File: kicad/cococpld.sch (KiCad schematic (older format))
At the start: 25 parts, among them P1 COCOBUS, P2 SPI, P3 JTAG, P4 TST, P5 TST, P6 TST, P7 TST, U1 TLV1117-33, U2 R1LP0108ESF-5SI, U5 EPM3256A-TQFP144, U6 50.00MHz

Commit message: v1.4 schematic and board with corrections
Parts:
- added C3: 0.1uF, symbol C
- U2: renamed from U5; symbol EPM3128A-TQFP144 -> EPM3256A-TQFP144
- renumbered C2 to C1, C10 to C2, C11 to C4, C7 to C5, C14 to C6, C8 to C7, C9 to C8, P5 to P1, P4 to P2, P1 to P3, P7 to P4, P6 to P5, P2 to P6, P3 to P7, U2 to U1, U6 to U3, U1 to U4
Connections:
- net labels added: C_A0, C_A1, C_A10, C_A11, C_A12, C_A13, C_A14, C_A2, C_A3, C_A4, C_A5, C_A6, C_A7, C_A8, C_A9, M_A0, M_A1, M_A10, M_A11, M_A12, M_A13, M_A14, M_A15, M_A2, M_A3, M_A4, M_A5, M_A6, M_A7, M_A8, M_A9
- net labels removed: A0, A1, A10, A11, A12, A13, A14, A15, A2, A3, A4, A5, A6, A7, A8, A9
- wire segments 72 -> 79
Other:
- moved on the sheet: C1, C2, C4, C5, C6, C7, C8, D1, D2, D3, D4, D5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

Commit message: refactored disk code - still working on RBF format and switching between disk formats.  Reads config from setup file.  CPLD code ported from FPGA but HW design still in progress.  Schematic in progress, including addition of wiznet support.
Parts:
- removed C1, C2, C3, C4, C5, C6: 0.1uF, symbol C
- removed JP1: CART_BOOT, symbol JUMPER
- removed P3: COCOBUS, symbol COCOBUS
- removed P6: SPI, symbol CONN_4X2
- removed P7: JTAG, symbol CONN_5X2
- removed U1: R1LP0108ESF-5SI, symbol R1LP0108ESF-5SI
- removed U2: EPM3256A-TQFP144, symbol EPM3256A-TQFP144
- removed U3: 50.00MHz, symbol OSC
- added P?: JTAG, symbol CONN_5X2
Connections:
- net labels removed: CLOCK_50, C_A0, C_A1, C_A10, C_A11, C_A12, C_A13, C_A14, C_A2, C_A3, C_A4, C_A5, C_A6, C_A7, C_A8, C_A9, C_D0, C_D1, C_D2, C_D3, C_D4, C_D5, C_D6, C_D7, C_ECLK, C_QCLK, C_R/~W, C_~CART, C_~CTS, C_~HALT, C_~NMI, C_~RESET, C_~SCS, C_~SLENB, DIRTY, MISO, MOSI, M_A0, M_A1, M_A10, M_A11, M_A12, M_A13, M_A14, M_A15, M_A2, M_A3, M_A4, M_A5, M_A6, M_A7, M_A8, M_A9, M_D0, M_D1, M_D2, M_D3, M_D4, M_D5, M_D6, M_D7, M_~CE, M_~OE, M_~WE, SCLK, ~RESET, ~SS
- wire segments 79 -> 60
- no-connect marks 7 -> 3
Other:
- moved on the sheet: C7, C8, D1, D2, D3, D4, D5, P1, P2, P4, P5, RP1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

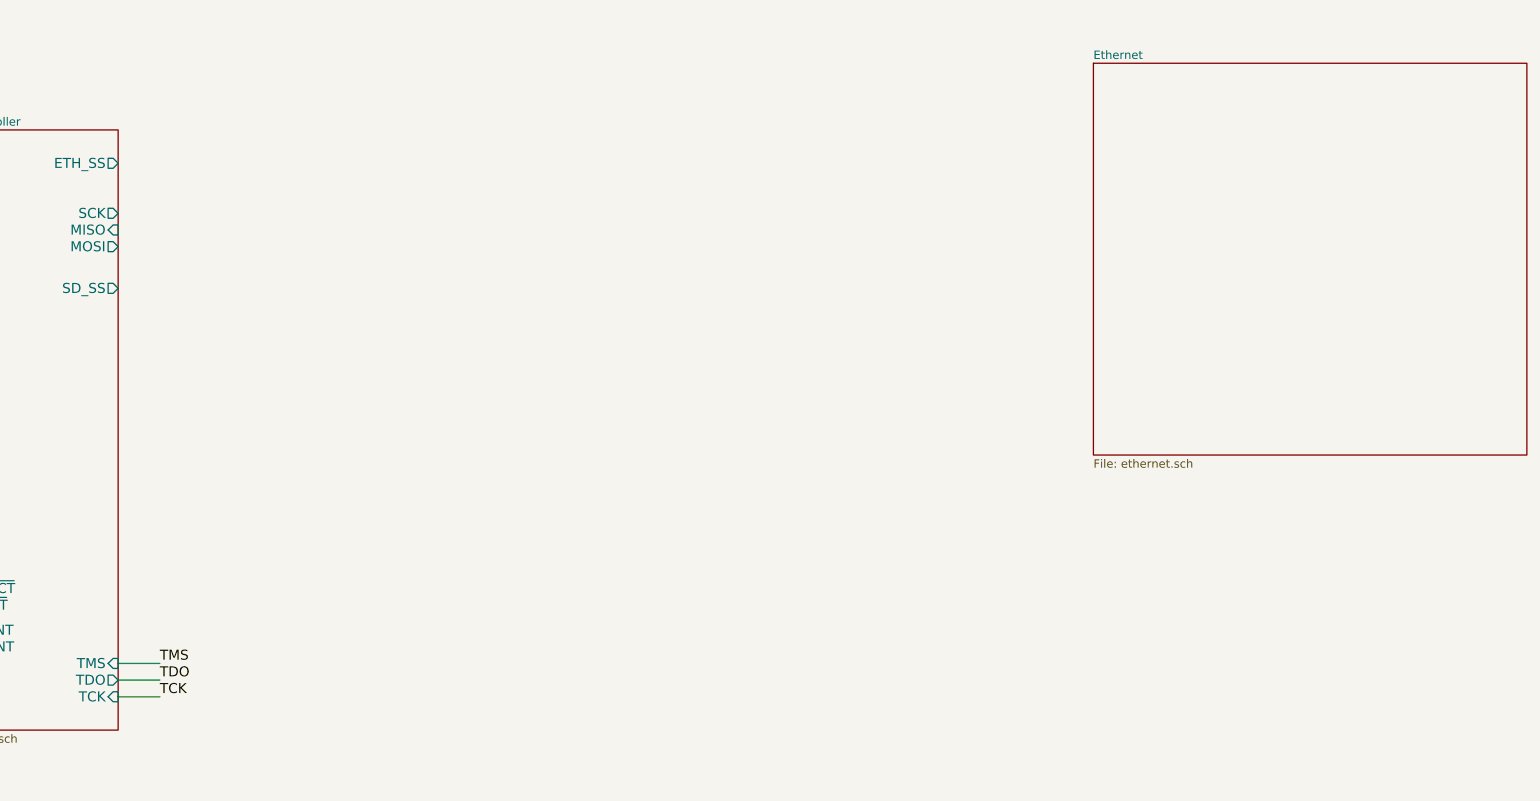
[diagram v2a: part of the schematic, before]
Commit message: added microsd and ethernet chip to design
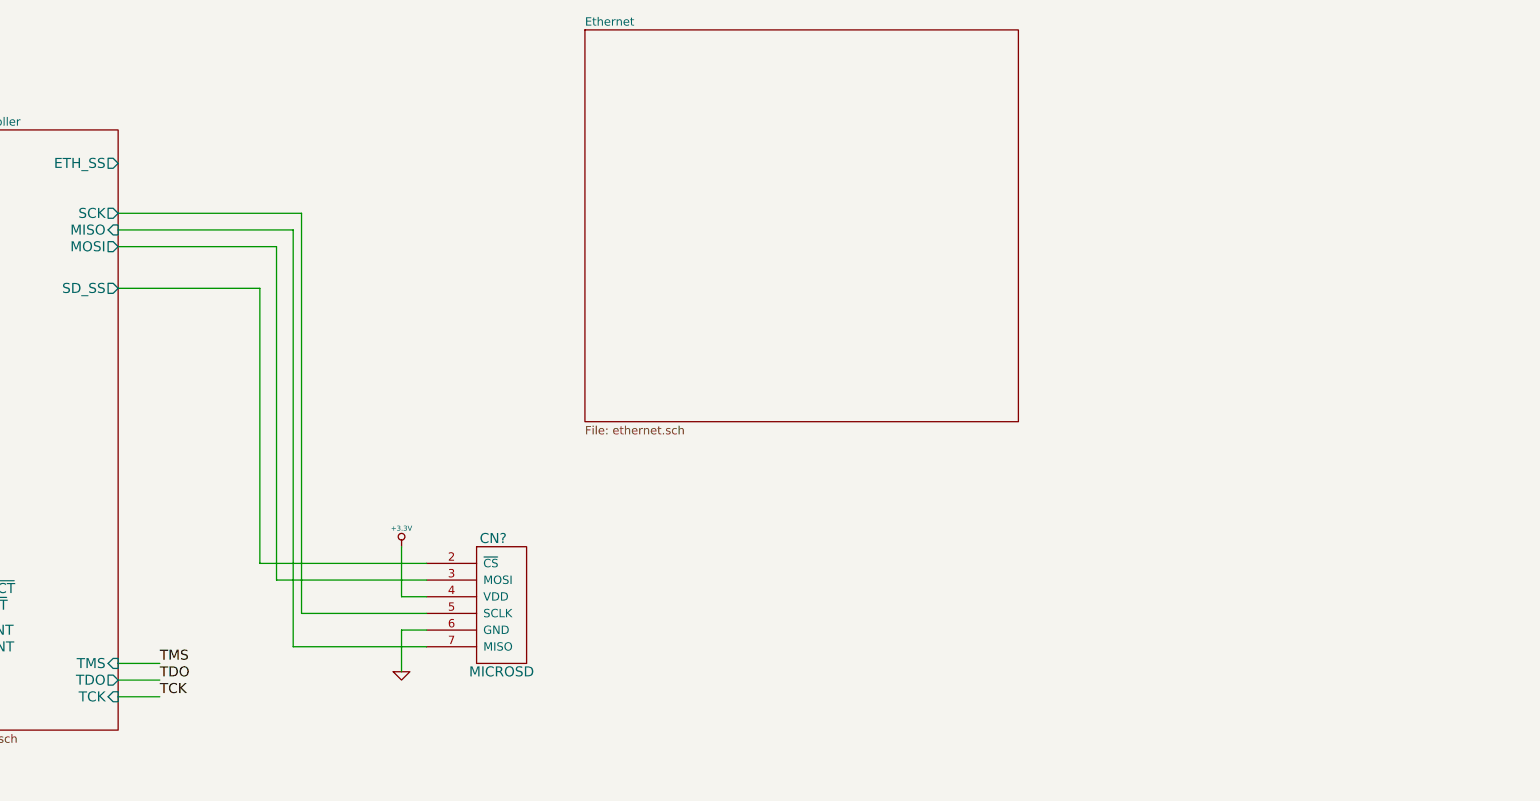
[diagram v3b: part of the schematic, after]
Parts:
- added CN?: MICROSD, symbol MICROSD
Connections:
- net +3.3V: now also CN?.4 (VDD)
- net GND: now also CN?.6 (GND)
- net Microcontroller/MISO: now also CN?.7 (MISO)
- net Microcontroller/MOSI: now also CN?.3 (MOSI)
- net Microcontroller/SCK: now also CN?.5 (SCLK)
- net Microcontroller/SD_SS: now also CN?.2 (~CS)
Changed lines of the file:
@@
 Sheet 1 4
 Title "Color Computer FDC Ethernet Controller"
-Date "4 jul 2013"
+Date "31 jul 2013"
 Rev "2.0"
 Comp "Bexkat Systems LLC 2013"
@@
 $EndSheet
 $Sheet
-S 9950 1600 2600 2350
+S 6900 1400 2600 2350
 U 51D5AFBF
 F0 "Ethernet" 50
@@
 Wire Wire Line
 	2250 5100 3000 5100
+$Comp
+L MICROSD CN?
+U 1 1 51F8FA6A
+P 6250 4850
+F 0 "CN?" H 6350 5250 60  0000 C CNN
+F 1 "MICROSD" H 6400 4450 60  0000 C CNN
+F 2 "" H 8000 3900 60  0000 C CNN
+F 3 "" H 8000 3900 60  0000 C CNN
+	1    6250 4850
+	1    0    0    -1
+$EndComp
+Wire Wire Line
+	4100 2950 4950 2950
+Wire Wire Line
+	4950 2950 4950 4600
+Wire Wire Line
+	4950 4600 5950 4600
+Wire Wire Line
+	4100 2700 5050 2700
+Wire Wire Line
+	5050 2700 5050 4700
+Wire Wire Line
+	5050 4700 5950 4700
+Wire Wire Line
+	4100 2600 5150 2600
+Wire Wire Line
+	5150 2600 5150 5100
+Wire Wire Line
+	5150 5100 5950 5100
+Wire Wire Line
+	4100 2500 5200 2500
+Wire Wire Line
+	5200 2500 5200 4900
+Wire Wire Line
+	5200 4900 5950 4900
+$Comp
+L GND #PWR?
+U 1 1 51F90ACD
+P 5800 5250
+F 0 "#PWR?" H 5800 5250 30  0001 C CNN
+F 1 "GND" H 5800 5180 30  0001 C CNN
+F 2 "" H 5800 5250 60  0001 C CNN
+F 3 "" H 5800 5250 60  0001 C CNN
+	1    5800 5250
+	1    0    0    -1
+$EndComp
+$Comp
+L +3.3V #PWR?
+U 1 1 51F90AD3
+P 5800 4500
+F 0 "#PWR?" H 5800 4460 30  0001 C CNN
+F 1 "+3.3V" H 5800 4610 30  0000 C CNN
+F 2 "" H 5800 4500 60  0001 C CNN
+F 3 "" H 5800 4500 60  0001 C CNN
+	1    5800 4500
+	1    0    0    -1
+$EndComp
+Wire Wire Line
+	5800 4500 5800 4800
+Wire Wire Line
+	5800 4800 5950 4800
+Wire Wire Line
+	5800 5250 5800 5000
+Wire Wire Line
+	5800 5000 5950 5000
 $EndSCHEMATC

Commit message: hardware prototype for v2.0 board
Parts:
- removed D1: S0, symbol LED
- removed D2: S1, symbol LED
- removed D3: S2, symbol LED
- removed D4: S3, symbol LED
- removed RP1: 150, symbol R_PACK4
- added C1: 10uF, symbol CP1
- added C2: 100uF, symbol CP1
- added D6, D7: DIODE, symbol DIODE
- added P12: BARREL_JACK, symbol BARREL_JACK
- added P13, P14: TST, symbol TST
- added P6: WIZNET J1, symbol CONN_10X2
- added P7: WIZNET J2, symbol CONN_10X2
- added P9: Mode, symbol CONN_3X2
- added R4: R, ~, symbol R
- added SW3: Reset, ~, symbol SW_PUSH
- added U1: TLV1117-50, symbol TLV1117-33
- gave numbers to parts that had none: 2
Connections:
- net +3.3V: now also P6.12 (P12), P7.1 (P1)
- net +5V: now also P9.4, R4.1
- net GND: now also C1.2, C2.2, P12.2, P6.11 (P11), P7.10 (P10), P7.19 (P19), P7.20 (P20), P7.9 (P9), SW3.2, U1.1 (GND)
- net Microcontroller/ETH_SS: now also P7.4 (P4)
- net Microcontroller/MISO: now also P6.2 (P2)
- net Microcontroller/MOSI renamed Coco interface/MOSI_33
- net Coco interface/MOSI_33: now also P6.1 (P1)
- net Microcontroller/SCK renamed Coco interface/SCLK_33
- net Coco interface/SCLK_33: now also P7.3 (P3)
- net Microcontroller/SD_SS renamed Coco interface/SD_SS_33
- new net: D7.1 (A), P12.1
- new net: C1.1, D6.2 (K), D7.2 (K), U1.3 (VI)
- new net: P9.5, R4.2, SW3.1
- new net C_POWER: P9.2
- new net C_RESET: P9.1
- new net EXT_REG5: C2.1, D6.1 (A), P9.6, U1.2 (VO)
- new net ~RESET: P7.2 (P2), P9.3
- no-connect marks 3 -> 31
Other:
- moved on the sheet: C7, C8, D5, P8, U4

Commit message: some changes
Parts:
- R4: value R -> 47k
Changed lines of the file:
@@
 P 11450 2750
 F 0 "R4" V 11530 2750 40  0000 C CNN
-F 1 "R" V 11457 2751 40  0000 C CNN
+F 1 "47k" V 11457 2751 40  0000 C CNN
 F 2 "~" V 11380 2750 30  0000 C CNN
 F 3 "~" H 11450 2750 30  0000 C CNN

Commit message: start of additional goodness and fixes
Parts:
- added D8: CP, symbol LED
- added D9: EP, symbol LED
- added P15: JTAG SEL, symbol CONN_3X2
- added P16: ICSP, symbol CONN_3X2
- added R3, R5: 150, ~, symbol R
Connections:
- net +5V: now also P16.2
- net C_POWER: now also R3.1
- net EXT_REG5: now also R5.1
- net GND: now also D8.2 (K), D9.2 (K), P16.6
- net TDI: now also P15.4
- net TDO: now also P15.3
- net ~RESET: now also P16.5
- net Microcontroller/MISO renamed MISO
- net MISO: now also P16.1
- new net: D8.1 (A), R3.2
- new net: D9.1 (A), R5.2
- new net A_TDI: P15.5
- new net A_TDO: P15.1
- new net C_TDI: P15.6
- new net C_TDO: P15.2
- new net MOSI: P16.4
- new net SCK: P16.3
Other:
- moved on the sheet: C1, C2, C7, C8, D5, D6, D7, P12, U1, U4

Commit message: eliminated header since JTAG chaining is confirmed to work.  Also drafted changes to firmware to support parallel mode I/O to CPLD instead of SPI as well as pure ROM mode.
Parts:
- removed P15: JTAG SEL, symbol CONN_3X2
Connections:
- net TDI is gone; now on net C_TDI: P3.9
- net TDO is gone; now on net A_TDO: P3.3
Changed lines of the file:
@@
 Sheet 1 3
 Title "Color Computer FDC Ethernet Controller"
-Date "20 aug 2013"
+Date "21 aug 2013"
 Rev "2.1"
 Comp "Bexkat Systems LLC 2013"
@@
 Text Label 2150 7050 2    60   ~ 0
 TMS
-Text Label 2150 6950 2    60   ~ 0
-TDO
-Text Label 2150 7250 2    60   ~ 0
-TDI
 $Comp
 L GND #PWR10
@@
 Wire Wire Line
 	5300 4850 7200 4850
-$Comp
-L CONN_3X2 P15
-U 1 1 5213B460
-P 4350 7000
-F 0 "P15" H 4350 7250 50  0000 C CNN
-F 1 "JTAG SEL" V 4350 7050 40  0000 C CNN
-F 2 "" H 4350 7000 60  0000 C CNN
-F 3 "" H 4350 7000 60  0000 C CNN
-	1    4350 7000
-	1    0    0    -1
-$EndComp
-Text Label 3950 6950 2    60   ~ 0
-TDO
-Text Label 4750 6950 0    60   ~ 0
-TDI
 Text Label 5300 5300 0    60   ~ 0
 C_TDO
 Text Label 7200 5300 2    60   ~ 0
 A_TDI
-Text Label 3950 6850 2    60   ~ 0
+Text Label 2150 6950 2    60   ~ 0
 A_TDO
-Text Label 4750 7050 0    60   ~ 0
+Text Label 2150 7250 2    60   ~ 0
 C_TDI
-Text Label 3950 7050 2    60   ~ 0
-A_TDI
-Text Label 4750 6850 0    60   ~ 0
-C_TDO
 $Comp
 L CONN_3X2 P16
@@
 Wire Wire Line
 	12200 5700 12200 6150
+Wire Wire Line
+	5300 5300 7200 5300
 $EndSCHEMATC
